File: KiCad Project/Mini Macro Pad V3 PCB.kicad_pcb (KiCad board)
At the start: 2 copper layers, 65 x 65 mm, 88 parts, among them J1 USB_C_Receptacle_USB2.0_14P, SW1 SW_Push bootsel, SW10 SW_Push, SW11 SW_Push, SW12 SW_Push, SW13 SW_Push, SW14 SW_Push, SW15 SW_Push, SW16 SW_Push, SW17 SW_Push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

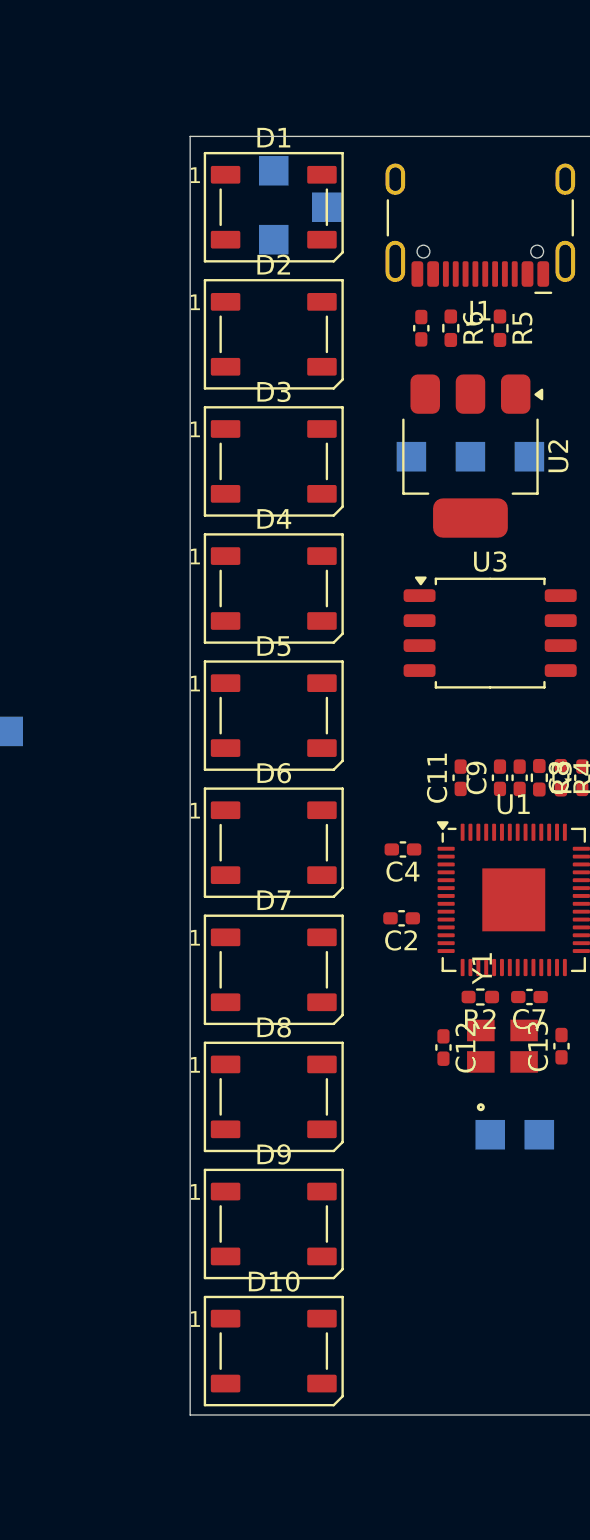
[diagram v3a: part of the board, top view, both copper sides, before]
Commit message: added decoupling capacitors for neopixels
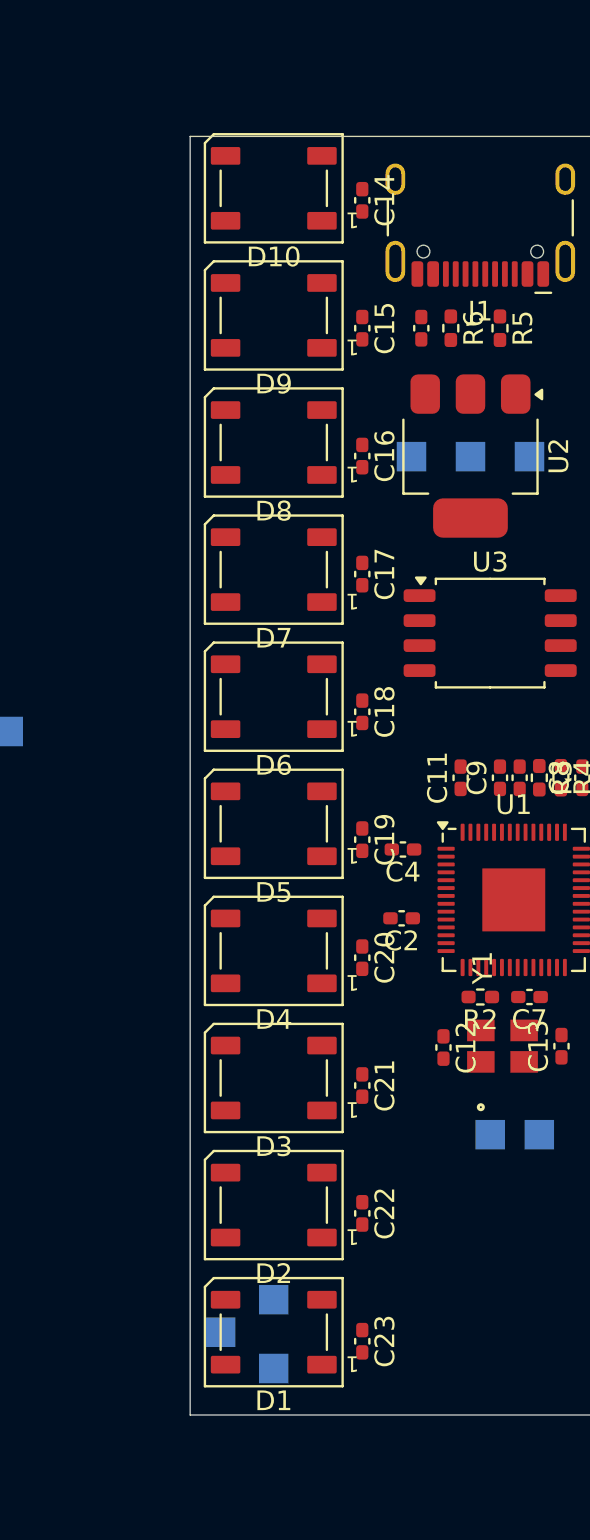
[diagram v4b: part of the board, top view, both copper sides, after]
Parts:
- added C14: 104, Capacitor_SMD:C_0402_1005Metric_Pad0.74x0.62mm_HandSolder, F.Cu at (111.5, 60.5)
- added C15: 104, Capacitor_SMD:C_0402_1005Metric_Pad0.74x0.62mm_HandSolder, F.Cu at (111.5, 67.0)
- added C16: 104, Capacitor_SMD:C_0402_1005Metric_Pad0.74x0.62mm_HandSolder, F.Cu at (111.5, 73.5)
- added C17: 104, Capacitor_SMD:C_0402_1005Metric_Pad0.74x0.62mm_HandSolder, F.Cu at (111.5, 79.5)
- added C18: 104, Capacitor_SMD:C_0402_1005Metric_Pad0.74x0.62mm_HandSolder, F.Cu at (111.5, 86.5)
- added C19: 104, Capacitor_SMD:C_0402_1005Metric_Pad0.74x0.62mm_HandSolder, F.Cu at (111.5, 93.0)
- added C20: 104, Capacitor_SMD:C_0402_1005Metric_Pad0.74x0.62mm_HandSolder, F.Cu at (111.5, 99.0)
- added C21: 104, Capacitor_SMD:C_0402_1005Metric_Pad0.74x0.62mm_HandSolder, F.Cu at (111.5, 105.5)
- added C22: 104, Capacitor_SMD:C_0402_1005Metric_Pad0.74x0.62mm_HandSolder, F.Cu at (111.5, 112.0)
- added C23: 104, Capacitor_SMD:C_0402_1005Metric_Pad0.74x0.62mm_HandSolder, F.Cu at (111.5, 118.5)
- moved TP18 60.9 mm to (107.0, 119.9), turned to 0 degrees
- moved D10 59.1 mm to (107.0, 59.9), turned to 180 degrees
- moved TP17 57.4 mm to (104.3, 118.0), turned to 0 degrees
- moved D1 57.2 mm to (107.0, 118.0), turned to 180 degrees
- moved TP19 53.9 mm to (107.0, 116.4), turned to 0 degrees
- moved D9 46.2 mm to (107.0, 66.3), turned to 180 degrees
- moved D2 44.3 mm to (107.0, 111.6), turned to 180 degrees
- moved D8 33.3 mm to (107.0, 72.8), turned to 180 degrees
- moved D3 31.3 mm to (107.0, 105.1), turned to 180 degrees
- moved D7 20.3 mm to (107.0, 79.3), turned to 180 degrees
- moved D4 18.4 mm to (107.0, 98.7), turned to 180 degrees
- moved D6 7.42 mm to (107.0, 85.7), turned to 180 degrees
- moved D5 5.50 mm to (107.0, 92.2), turned to 180 degrees

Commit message: Started drawing traces
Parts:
- C5, C9: moved to B.Cu
- SW22, SW23: footprint Rotary_Encoder:RotaryEncoder_Bourns_Horizontal_PEL12D-2x16F-Sxxxx -> Rotary_Encoder:RotaryEncoder_Bourns_Horizontal_PEC12R-2x17F-Sxxxx
- moved TP12 43.4 mm to (124.0, 119.0)
- moved TP13 42.0 mm to (114.0, 108.3)
- moved TP14 41.1 mm to (114.0, 111.4)
- moved TP8 41.1 mm to (117.5, 108.3)
- moved TP6 40.7 mm to (124.0, 114.5)
- moved TP9 40.3 mm to (117.5, 111.4)
- moved TP15 40.2 mm to (113.5, 115.0)
- moved TP16 39.7 mm to (113.5, 118.5)
- moved TP4 39.4 mm to (121.0, 111.3)
- moved TP3 39.4 mm to (120.0, 108.3)
- moved TP10 39.3 mm to (117.0, 115.0)
- moved TP11 38.8 mm to (117.0, 118.5)
- moved TP5 38.4 mm to (120.5, 114.9)
- moved TP7 35.5 mm to (120.0, 119.0)
- moved TP1 6.71 mm to (124.0, 111.0)
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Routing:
- net /MATRIX_R2: track 0.00 -> 72.8 mm
- net /MATRIX_R3: track 0.00 -> 72.8 mm
- net /MATRIX_R1: track 0.00 -> 72.4 mm
- net /MATRIX_R4: track 0.00 -> 72.3 mm
- net /MATRIX_R5: track 0.00 -> 72.2 mm
- net /ENCODER_2_B: track 0.00 -> 57.1 mm, vias 0 -> 1
- net /MATRIX_C1: track 0.00 -> 52.9 mm
- net /MATRIX_C3: track 0.00 -> 52.8 mm
- net /MATRIX_C2: track 0.00 -> 52.8 mm
- net /ENCODER_2_A: track 0.00 -> 52.2 mm, vias 0 -> 1
- net /MATRIX_C4: track 0.00 -> 51.7 mm
- net /ENCODER_2_S1: track 0.00 -> 50.4 mm, vias 0 -> 1
- net /ENCODER_1_B: track 0.00 -> 37.2 mm, vias 0 -> 1
- net +3.3V: track 0.00 -> 34.4 mm
- net /ENCODER_1_S1: track 0.00 -> 32.9 mm, vias 0 -> 1
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
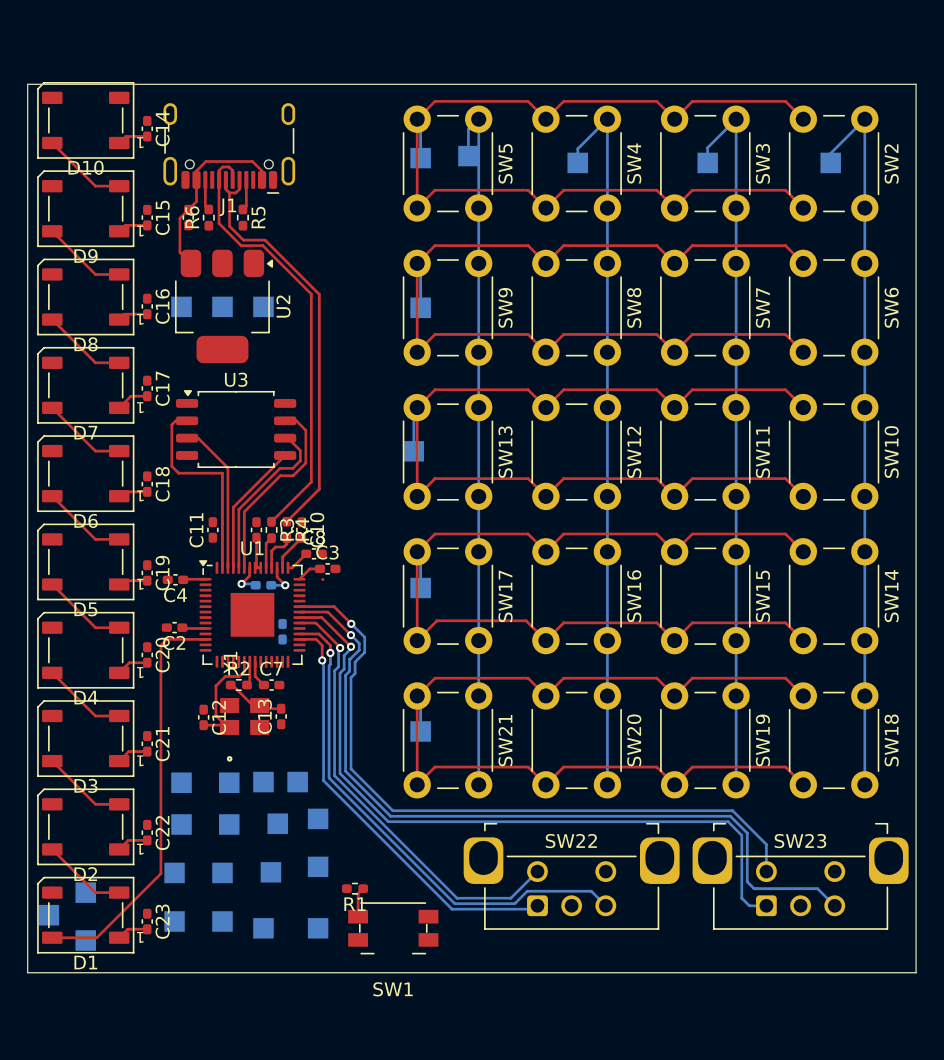
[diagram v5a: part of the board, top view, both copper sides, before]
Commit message: changed some GPIO connections & did more trace routing
Reversed the order that C1 to C5 connect in
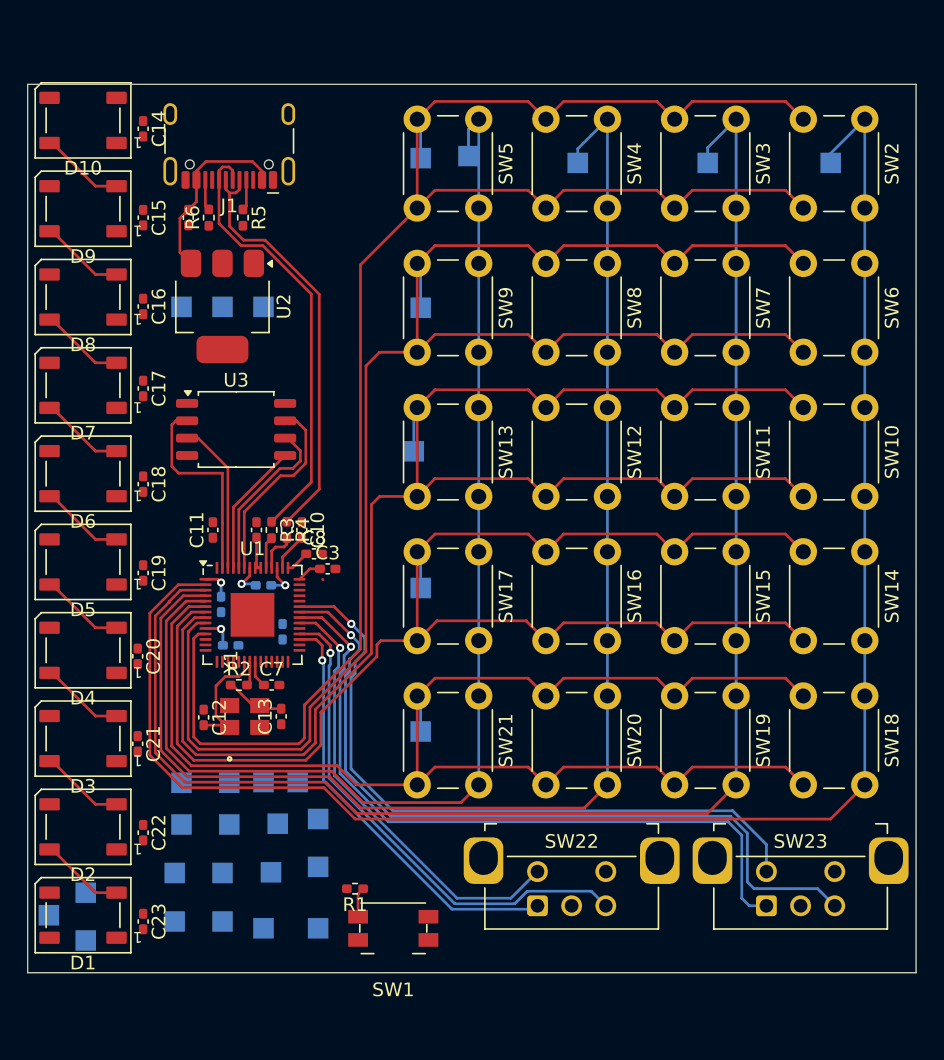
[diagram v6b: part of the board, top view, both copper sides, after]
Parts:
- C2, C4: moved to B.Cu
- moved C2 4.30 mm to (117.6, 98.3), turned to 0 degrees
- moved C4 3.79 mm to (116.9, 95.3), turned to -90 degrees
- moved C20 0.71 mm to (110.8, 99.1)
- moved C21 0.70 mm to (110.8, 105.5)
- moved C14 0.30 mm to (111.2, 60.5)
- moved C15 0.30 mm to (111.2, 67.0)
- moved C16 0.30 mm to (111.2, 73.5)
- moved C17 0.30 mm to (111.2, 79.5)
- moved C18 0.30 mm to (111.2, 86.5)
- moved C19 0.30 mm to (111.2, 93.0)
- moved C22 0.30 mm to (111.2, 112.0)
- moved C23 0.30 mm to (111.2, 118.5)
- moved D1 0.20 mm to (106.8, 118.0)
- moved D10 0.20 mm to (106.8, 59.9)
- moved D2 0.20 mm to (106.8, 111.6)
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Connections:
- U1 pad 11: /MATRIX_R5 -> /MATRIX_R1
- U1 pad 6: /MATRIX_R1 -> /MATRIX_R5
- U1 pad 7: /MATRIX_R2 -> /MATRIX_R4
- U1 pad 9: /MATRIX_R4 -> /MATRIX_R2
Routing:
- net /MATRIX_C1: track 52.9 -> 123.5 mm
- net /MATRIX_C2: track 52.8 -> 112.5 mm
- net /MATRIX_R1: track 72.4 -> 131.3 mm
- net /MATRIX_R2: track 72.8 -> 125.0 mm
- net /MATRIX_C3: track 52.8 -> 101.6 mm
- net /MATRIX_R3: track 72.8 -> 116.2 mm
- net /MATRIX_C4: track 51.7 -> 89.5 mm
- net /MATRIX_R4: track 72.3 -> 107.3 mm
- net /MATRIX_R5: track 72.2 -> 103.2 mm
- net /NEOPIXEL_DIN: track 30.0 -> 0.00 mm
- net +3.3V: track 34.4 -> 13.7 mm, vias 0 -> 2

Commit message: more routing traces.
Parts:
- C2, C4, C5: moved to F.Cu
- moved C11 12.1 mm to (121.0, 78.7), turned to 180 degrees
- moved R1 4.70 mm to (131.4, 116.1)
- moved C4 3.74 mm to (113.8, 93.2), turned to 180 degrees
- moved C5 3.47 mm to (123.9, 99.7)
- moved C2 3.28 mm to (115.6, 100.9), turned to -90 degrees
- moved C21 2.40 mm to (110.9, 107.9), turned to 90 degrees
- moved C20 2.30 mm to (110.8, 101.4), turned to 90 degrees
- moved TP22 0.52 mm to (114.5, 73.4)
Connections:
- R1 pad 2: +3.3V -> /QSPI_SS
- U1 pad 56: +3.3V -> /QSPI_SS
- U3 pad 1: +3.3V -> /QSPI_SS
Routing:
- net /QSPI_SS: track 0.00 -> 58.8 mm
- net /NEOPIXEL_DIN: track 0.00 -> 29.8 mm, vias 0 -> 2
- net +3.3V: track 13.7 -> 31.6 mm, vias 2 -> 0
- net Net-(C13-Pad2): track 4.42 -> 3.46 mm
- net /ENCODER_2_S1: track 50.4 -> 51.4 mm
- net /MATRIX_R4: track 107.3 -> 106.7 mm

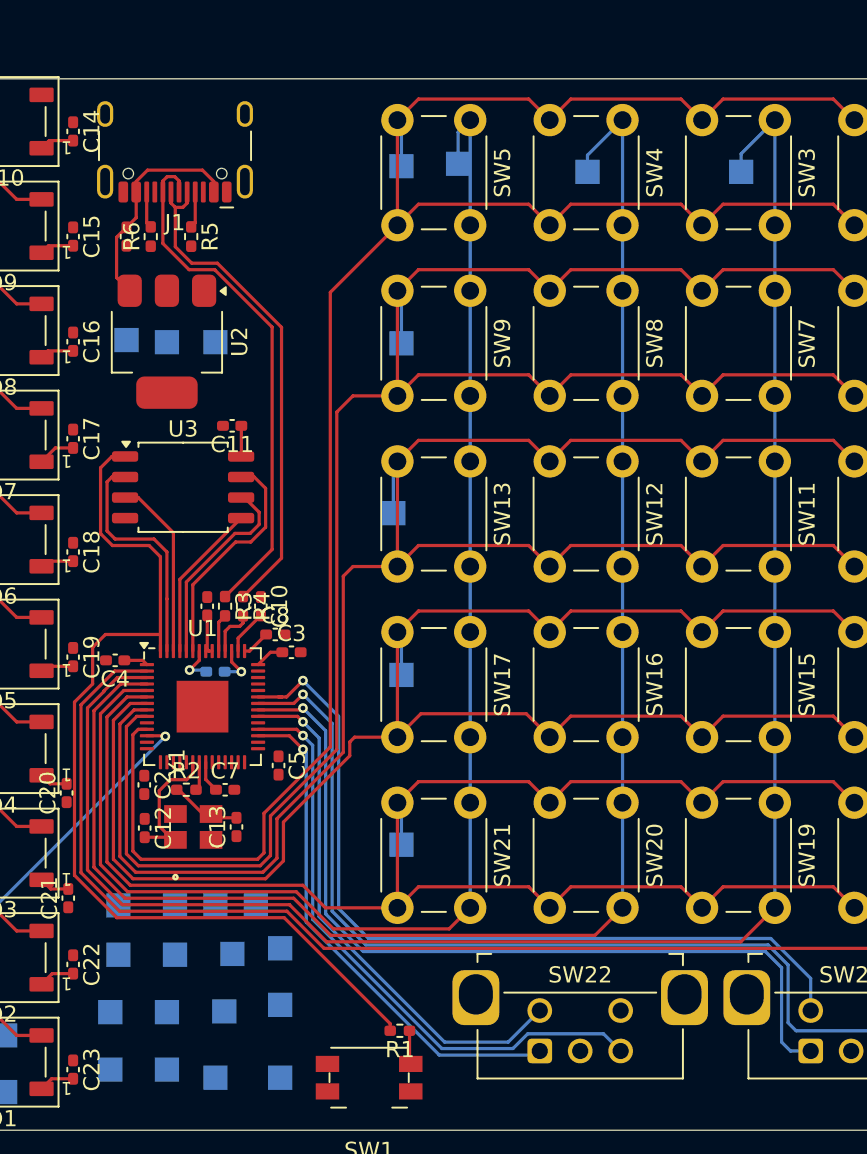
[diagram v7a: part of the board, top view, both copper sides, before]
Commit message: added ground and power planes
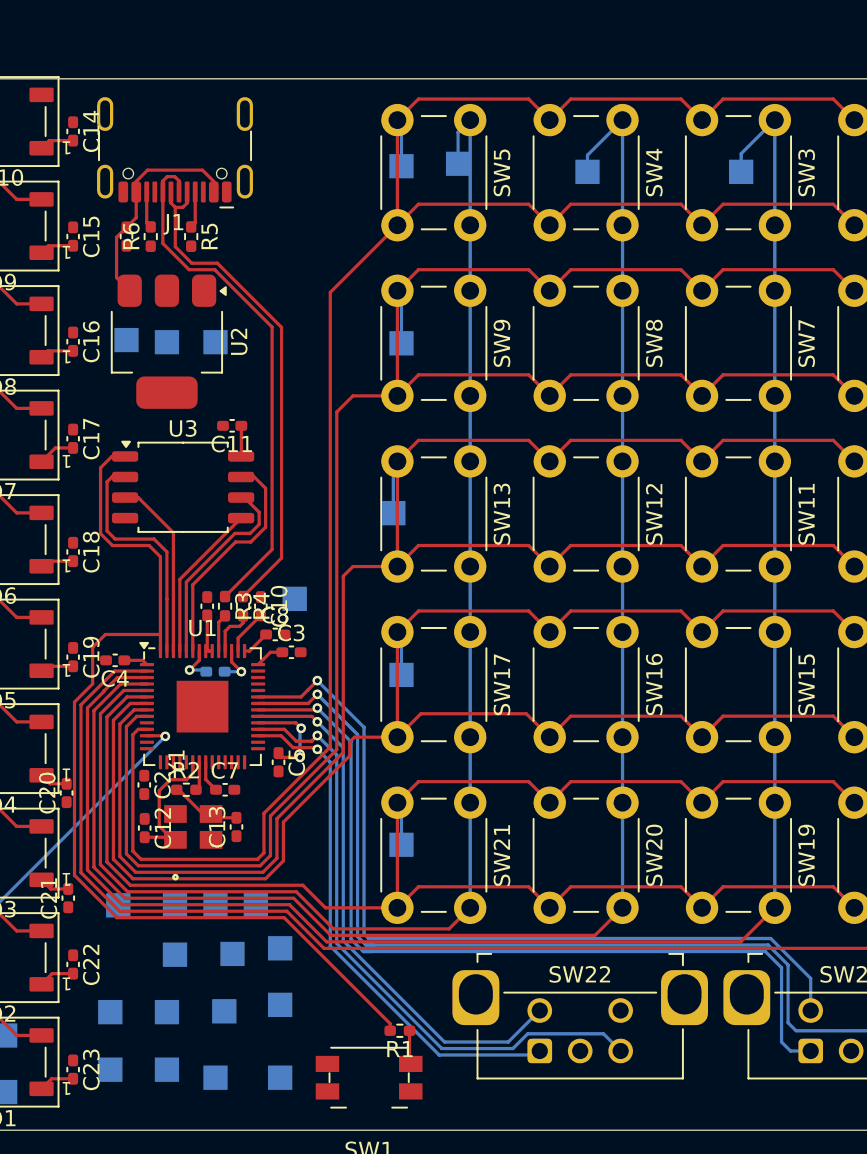
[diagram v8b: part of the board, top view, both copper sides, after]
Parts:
- moved TP14 24.6 mm to (124.9, 89.4)
- moved C5 0.20 mm to (123.9, 99.5)
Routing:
- net +3.3V: track 31.6 -> 37.9 mm, vias 0 -> 2
- net /ENCODER_2_A: track 52.3 -> 53.4 mm
- net /ENCODER_2_B: track 57.4 -> 58.4 mm
- net /ENCODER_1_B: track 37.7 -> 38.5 mm
- net /ENCODER_1_A: track 31.5 -> 32.0 mm
- net /ENCODER_1_S1: track 33.0 -> 33.5 mm
- added copper zone on In2.Cu, net +3.3V
- added copper zone on In1.Cu, net GND
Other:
- copper layers 2 -> 4
